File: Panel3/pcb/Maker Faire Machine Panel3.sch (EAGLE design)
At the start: 40 parts, among them IC1 TJA1049

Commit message: Update Panel 3 PCB after Eric's comments
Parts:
- Q1, Q2: device SparkFun-DiscreteSemi:TRANSISTOR_NPNTO92 -> SparkFun-DiscreteSemi:TRANSISTOR_NPNTO-92-AMMO
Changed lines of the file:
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@@
 <parts>
 <part name="U$1" library="Particle-Devices" deviceset="PHOTON_SMD" device=""/>
-<part name="Q1" library="SparkFun-DiscreteSemi" deviceset="TRANSISTOR_NPN" device="TO92">
+<part name="Q1" library="SparkFun-DiscreteSemi" deviceset="TRANSISTOR_NPN" device="TO-92-AMMO">
 <attribute name="PARTNO" value="PN2222ABU"/>
 </part>
@@
 <attribute name="PARTNO" value="OSTTE030104"/>
 </part>
-<part name="Q2" library="SparkFun-DiscreteSemi" deviceset="TRANSISTOR_NPN" device="TO92">
+<part name="Q2" library="SparkFun-DiscreteSemi" deviceset="TRANSISTOR_NPN" device="TO-92-AMMO">
 <attribute name="PARTNO" value="PN2222ABU"/>
 </part>

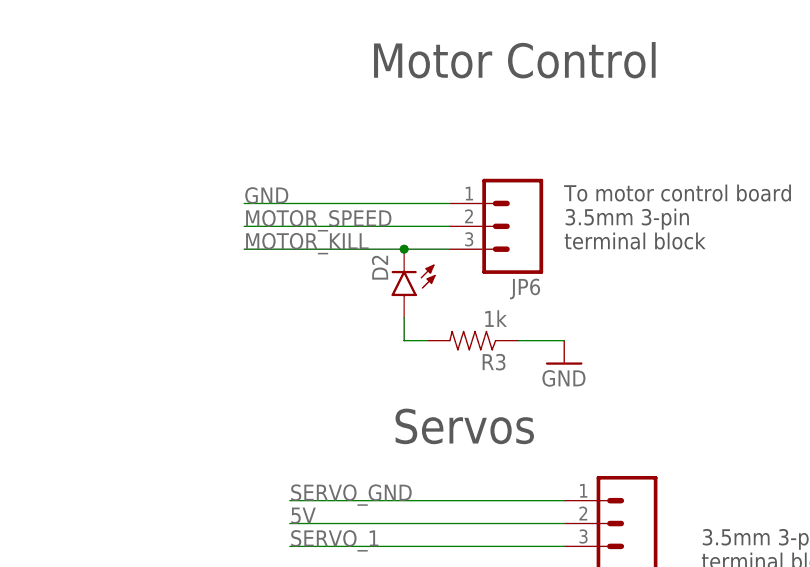
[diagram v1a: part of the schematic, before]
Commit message: Fix LED orientation
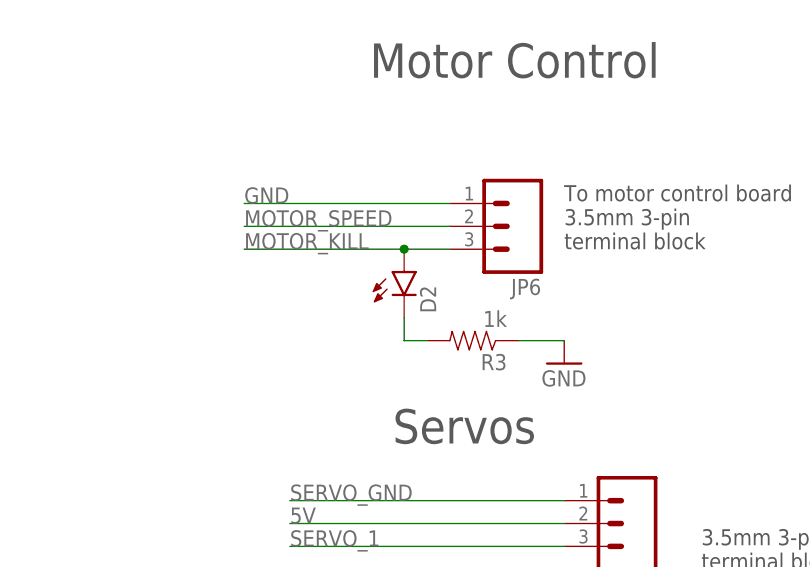
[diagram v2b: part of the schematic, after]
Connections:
- net MOTOR_KILL: now also D2.A; no longer D2.C
- net N$5: now also D2.C; no longer D2.A
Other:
- moved on the sheet: D2
